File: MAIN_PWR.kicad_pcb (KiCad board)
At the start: 2 copper layers, 128 x 127 mm, 316 parts, among them CN101 Conn_01x04_Socket, CN102 Conn_01x12_Socket, IC101 CXA1081, IC102 CXA1082BQ, IC103 RC4558, IC104 BA6290A, IC105 BA6290A, IC106 CXD1167Q, IC107 D4364G, IC108 D78C14GF, IC109 D6378GF, IC201 LC7881M, IC202 RC4560, IC203 RC4558, IC204 RC4558, IC301 L7805, IC302 1951A, P101 Conn_01x10, P102 Conn_01x11, P105 Conn_01x11, P107 Conn_01x11, Q101 Q_PNP_Darlington_BCEC, Q102 DTC114EU3, Q103 2SC2412K, Q104 2SC2412K, Q105 DTC114EU3, Q201 2SC2412K, Q202 2SC2412K, Q203 DTA124EU3, Q204 DTA124EU3, Q205 Q_NPN_BEC, Q206 Q_NPN_BEC, Q207 DTC114EU3, Q208 Q_NPN_BEC, Q209 Q_NPN_BEC, Q302 2SC2412K, Q307 2SC2412K, Q601 Q_NPN_BEC, Q602 Q_NPN_BEC

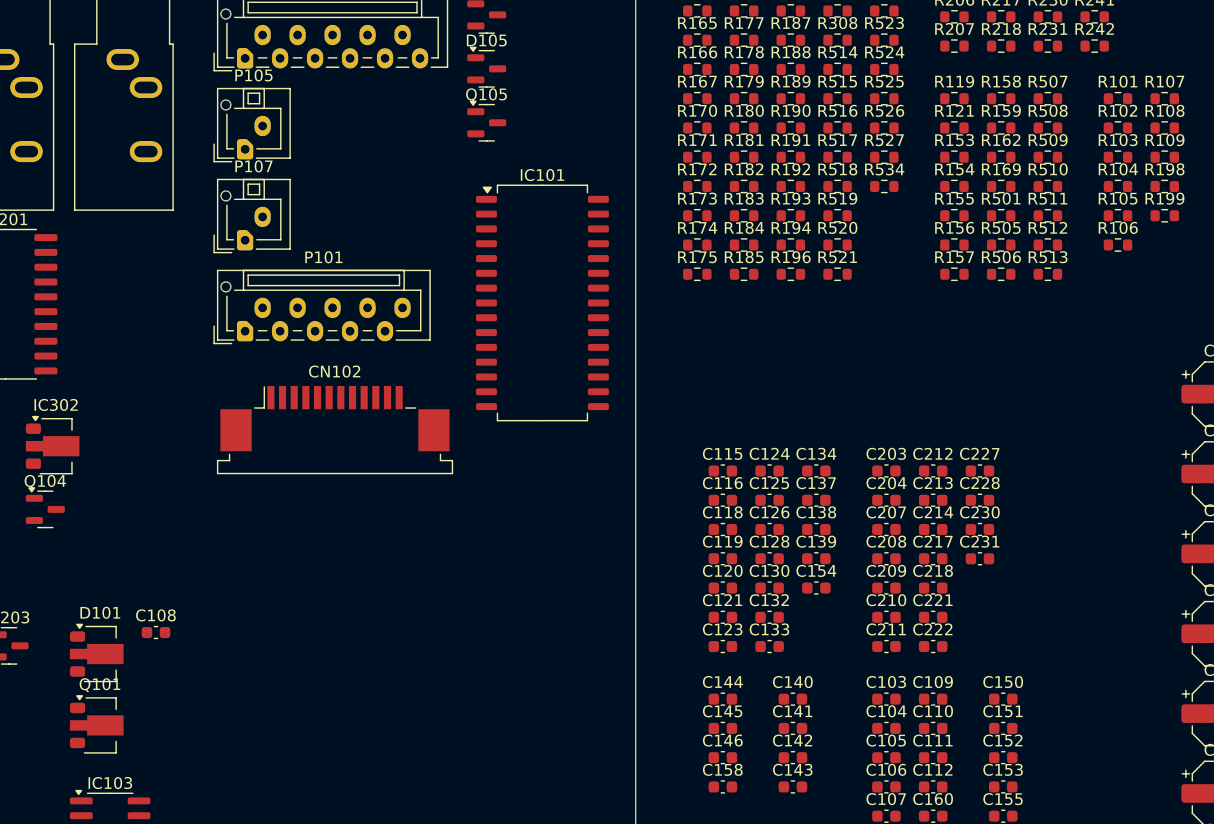
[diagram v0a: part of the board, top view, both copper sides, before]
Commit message: Small Schematics update to tidy signals attached to SCSI and MCU chips.
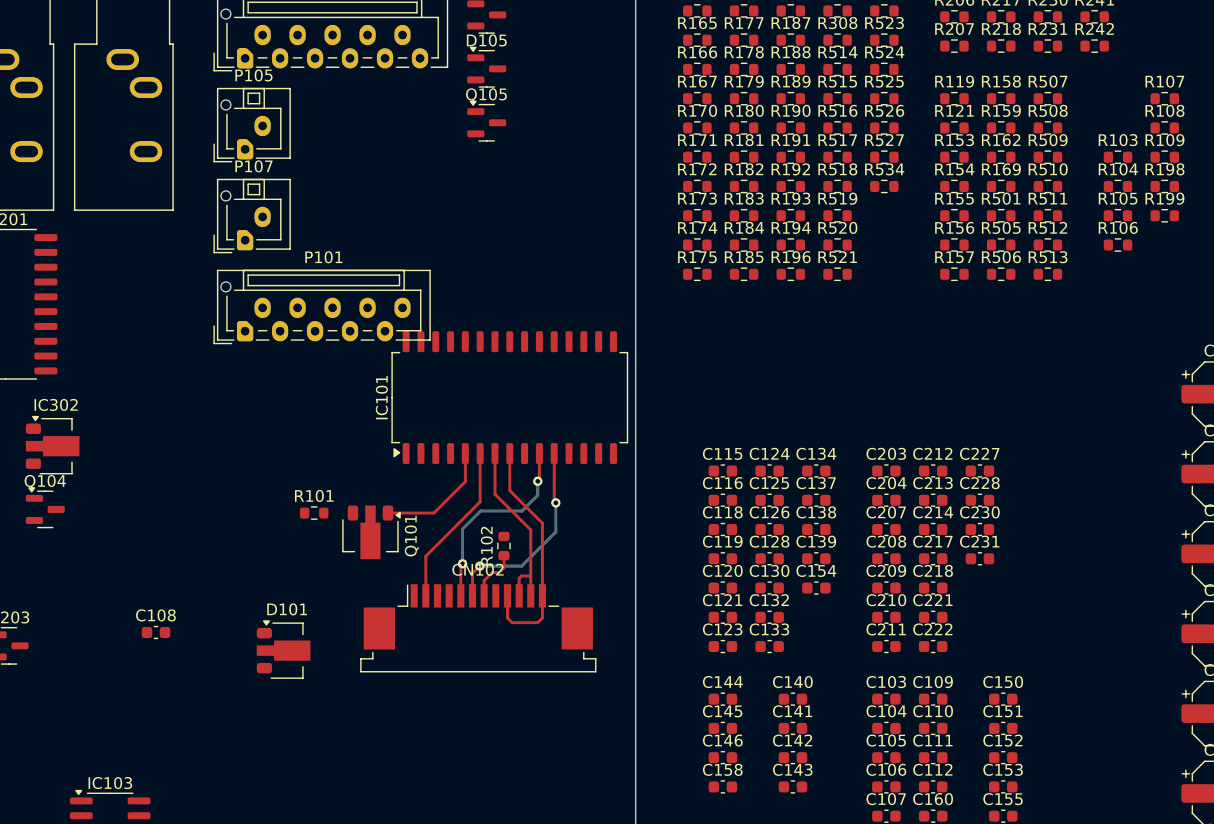
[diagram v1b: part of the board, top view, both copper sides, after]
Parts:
- moved R101 77.6 mm to (150.4, 112.6)
- moved R102 63.7 mm to (166.7, 115.4), turned to 90 degrees
- moved Q101 28.3 mm to (155.2, 114.5), turned to -90 degrees
- moved CN102 21.0 mm to (164.5, 121.5)
- moved D101 16.0 mm to (148.1, 124.4)
- moved IC101 8.59 mm to (167.2, 102.7), turned to 90 degrees
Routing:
- net /RF AMP/B+D: track 0.00 -> 20.5 mm
- net Net-(CN102-Pin_6): track 0.00 -> 17.3 mm, vias 0 -> 2
- net Net-(CN102-Pin_5): track 0.00 -> 17.1 mm, vias 0 -> 2
- net /RF AMP/A+C: track 0.00 -> 16.1 mm
- net Net-(CN102-Pin_2): track 0.00 -> 14.1 mm
- net Net-(IC101-LD): track 0.00 -> 10.2 mm
- net Net-(CN102-Pin_7): track 0.00 -> 4.51 mm
